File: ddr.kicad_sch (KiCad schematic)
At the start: 29 parts, among them U1 MIMX8MM6DVTLZAA, U2 MT40A1G16KD-062E

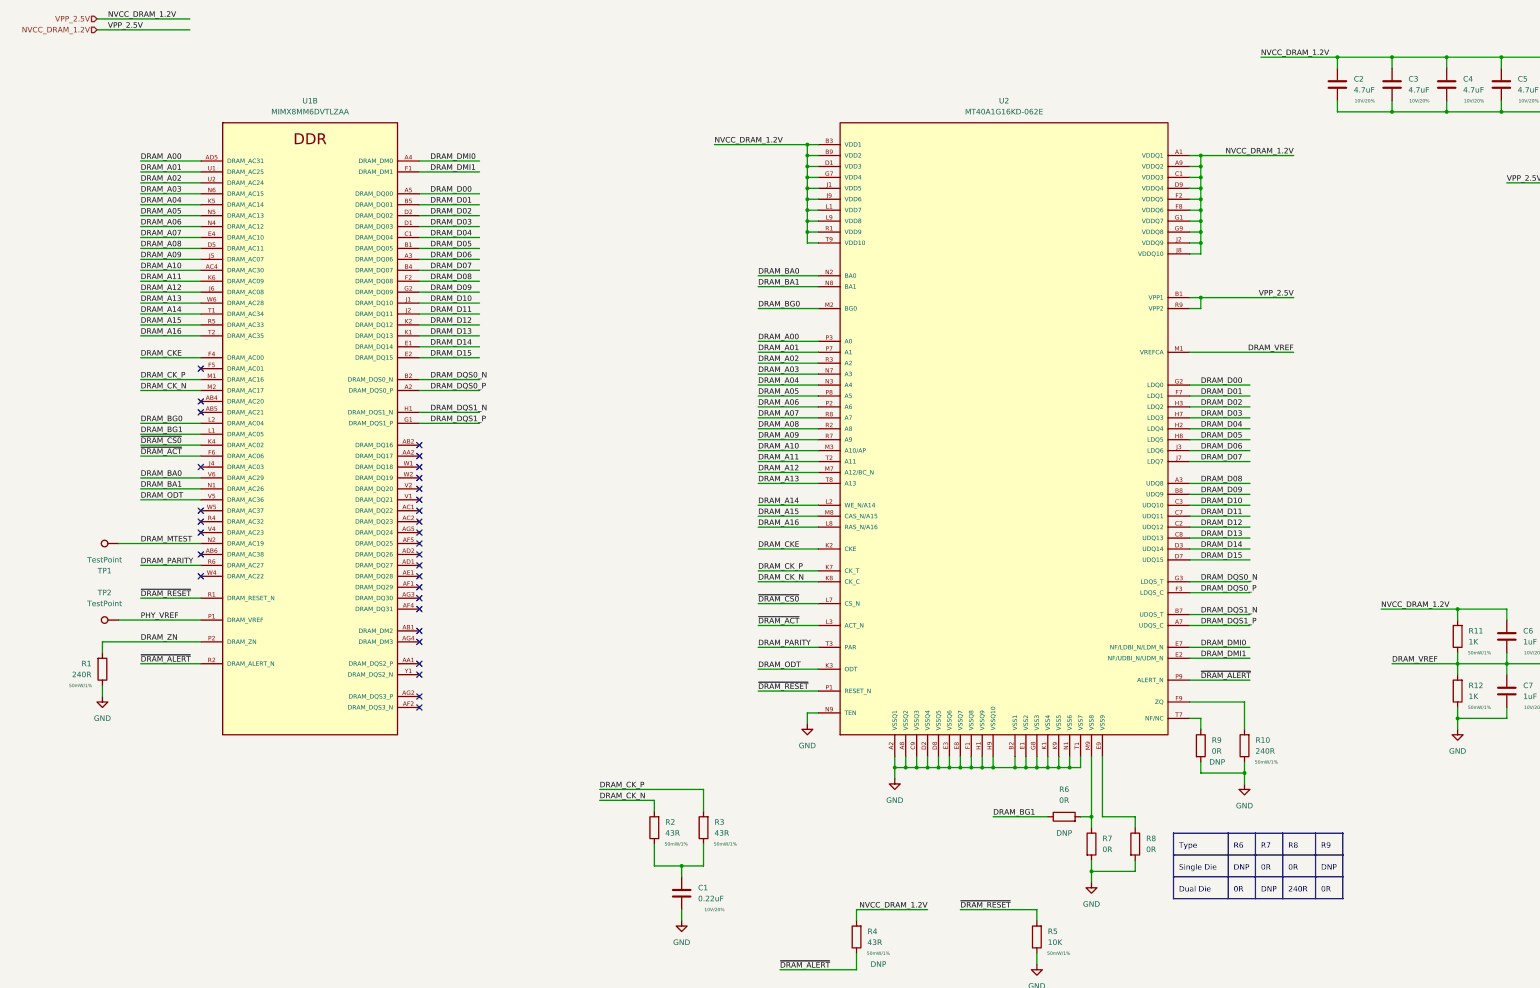
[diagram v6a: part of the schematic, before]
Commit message: add inital ddr tool version, lots of routing work
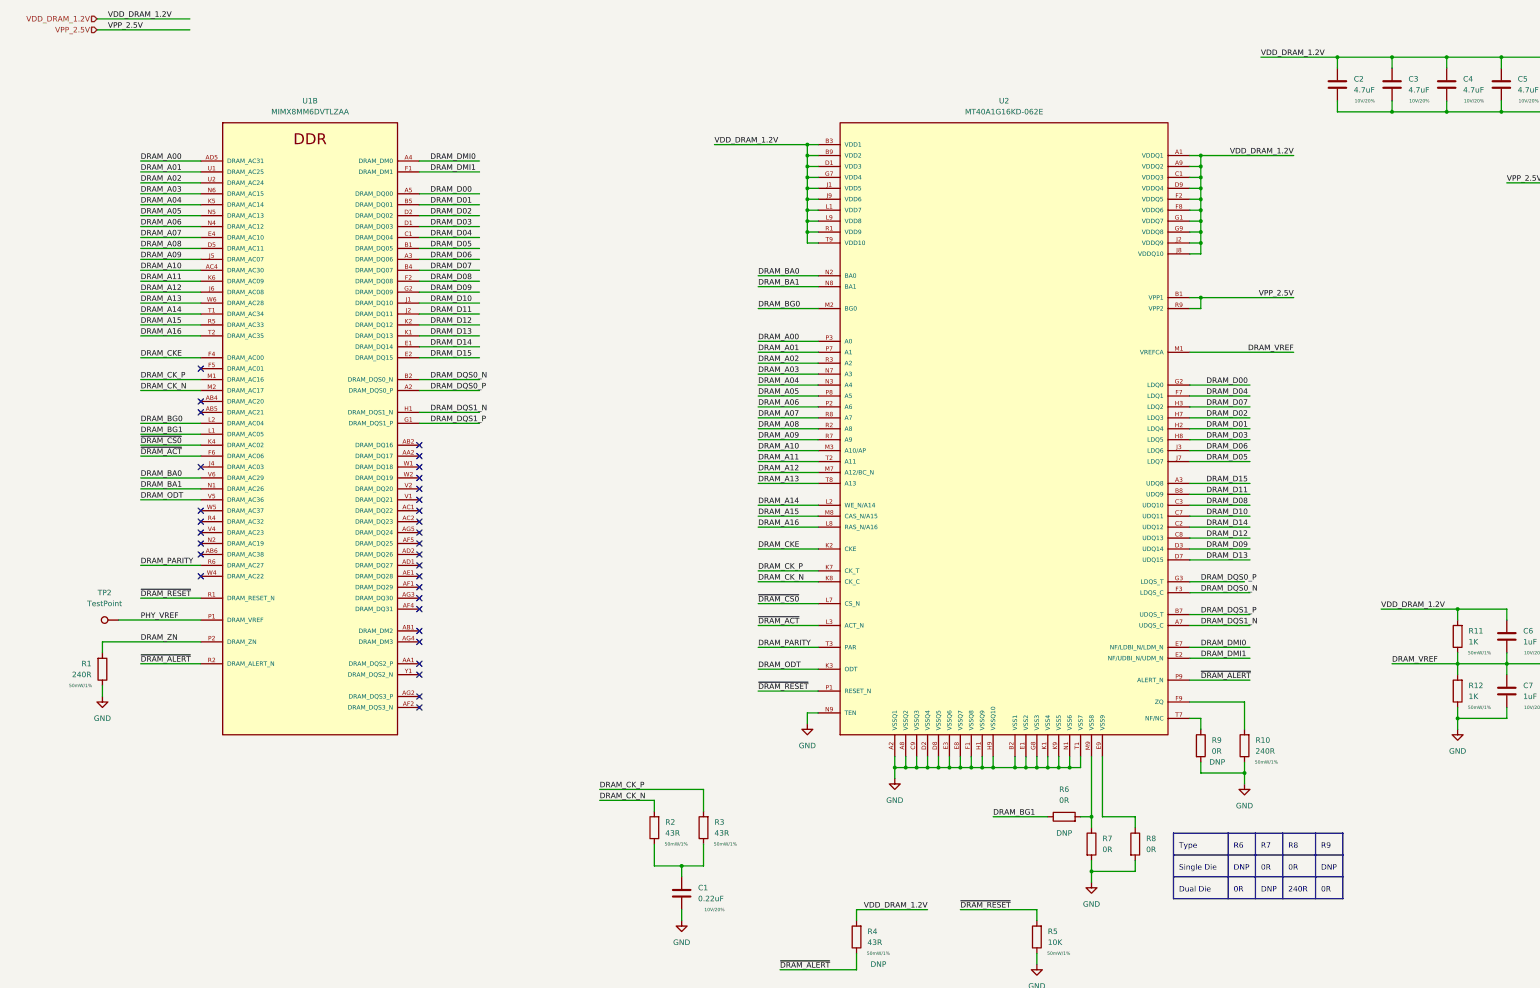
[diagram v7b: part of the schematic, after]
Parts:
- removed TP1: TestPoint, TestPoint:TestPoint_Pad_D1.0mm, symbol Connector:TestPoint
- C1, C12: footprint Capacitor_SMD:C_0201_0603Metric -> qsbc:C_0201_0603Metric
- R1, R10, R2, R3, R4: footprint Resistor_SMD:R_0201_0603Metric -> qsbc:R_0201_0603Metric
- R6, R7, R8, R9: footprint Resistor_SMD:R_0402_1005Metric -> qsbc:R_0201_0603Metric
- TP2: footprint TestPoint:TestPoint_Pad_D1.0mm -> qsbc:TestPoint_Pad_D0.4mm
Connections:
- net DRAM_D01: now also U2.H2 (LDQ4); no longer U2.F7 (LDQ1)
- net DRAM_D02: now also U2.H7 (LDQ3); no longer U2.H3 (LDQ2)
- net DRAM_D03: now also U2.H8 (LDQ5); no longer U2.H7 (LDQ3)
- net DRAM_D04: now also U2.F7 (LDQ1); no longer U2.H2 (LDQ4)
- net DRAM_D05: now also U2.J7 (LDQ7); no longer U2.H8 (LDQ5)
- net DRAM_D07: now also U2.H3 (LDQ2); no longer U2.J7 (LDQ7)
- net DRAM_D08: now also U2.C3 (UDQ10); no longer U2.A3 (UDQ8)
- net DRAM_D09: now also U2.D3 (UDQ14); no longer U2.B8 (UDQ9)
- net DRAM_D10: now also U2.C7 (UDQ11); no longer U2.C3 (UDQ10)
- net DRAM_D11: now also U2.B8 (UDQ9); no longer U2.C7 (UDQ11)
- net DRAM_D12: now also U2.C8 (UDQ13); no longer U2.C2 (UDQ12)
- net DRAM_D13: now also U2.D7 (UDQ15); no longer U2.C8 (UDQ13)
- net DRAM_D14: now also U2.C2 (UDQ12); no longer U2.D3 (UDQ14)
- net DRAM_D15: now also U2.A3 (UDQ8); no longer U2.D7 (UDQ15)
- net DRAM_DQS0_N: now also U2.F3 (LDQS_C); no longer U2.G3 (LDQS_T)
- net DRAM_DQS0_P: now also U2.G3 (LDQS_T); no longer U2.F3 (LDQS_C)
- net DRAM_DQS1_N: now also U2.A7 (UDQS_C); no longer U2.B7 (UDQS_T)
- net DRAM_DQS1_P: now also U2.B7 (UDQS_T); no longer U2.A7 (UDQS_C)
- net DRAM_MTEST: no longer names the net of U1.N2 (DRAM_AC19)
- net NVCC_DRAM_1.2V renamed VDD_DRAM_1.2V
- net VDD_DRAM_1.2V: no longer C11.1, C9.1, U2.B1 (VPP1), U2.R9 (VPP2)
- new net VPP_2.5V: C11.1, C9.1, U2.B1 (VPP1), U2.R9 (VPP2)
- no-connect marks 31 -> 32

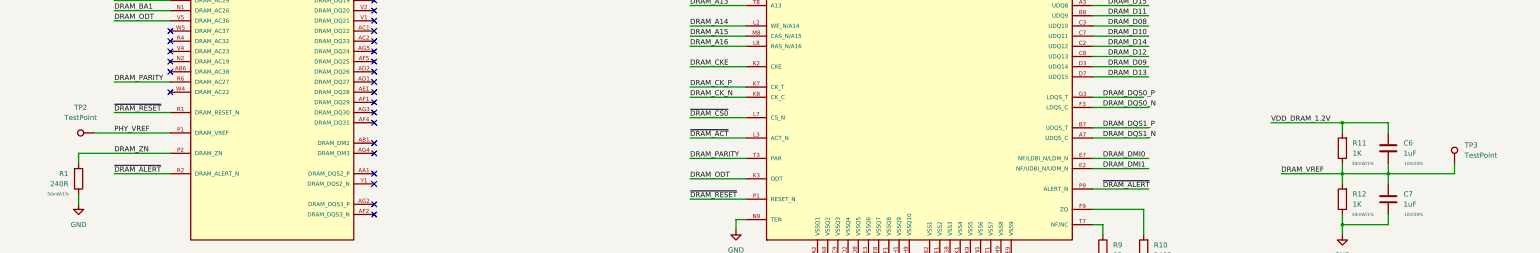
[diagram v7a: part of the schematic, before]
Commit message: v2 of ddr flytimes tool, lots of routing work, sch fixes
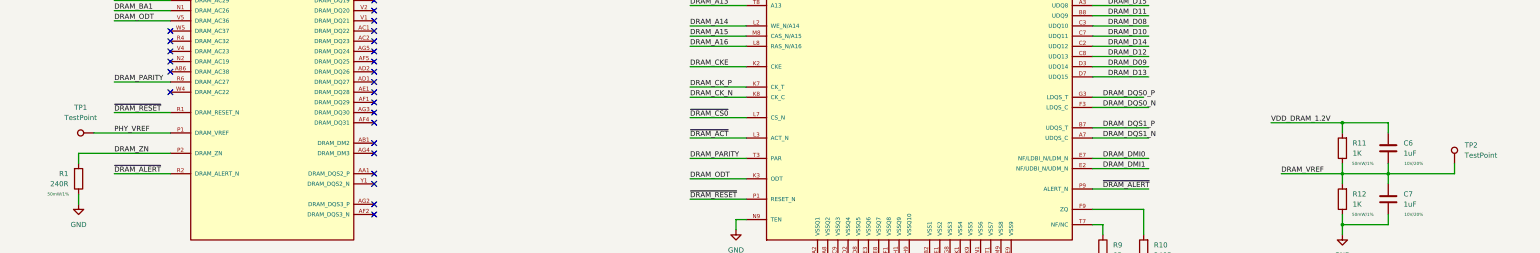
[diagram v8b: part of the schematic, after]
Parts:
- renumbered TP2 to TP1, TP3 to TP2
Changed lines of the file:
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@@
   (symbol (lib_id "Connector:TestPoint") (at 45.72 163.83 90) (mirror x) (unit 1)
     (in_bom yes) (on_board yes)
-    (property "Reference" "TP2" (id 0) (at 42.418 157.48 90))
+    (property "Reference" "TP1" (id 0) (at 42.418 157.48 90))
     (property "Value" "TestPoint" (id 1) (at 42.418 160.02 90))
     (property "Footprint" "qsbc:TestPoint_Pad_D0.4mm" (id 2) (at 45.72 168.91 0)
@@
   (symbol (lib_id "Connector:TestPoint") (at 384.81 171.45 0) (unit 1)
     (in_bom yes) (on_board yes) (fields_autoplaced)
-    (property "Reference" "TP3" (id 0) (at 387.35 166.8779 0)
+    (property "Reference" "TP2" (id 0) (at 387.35 166.8779 0)
       (effects (font (size 1.27 1.27)) (justify left))
     )
